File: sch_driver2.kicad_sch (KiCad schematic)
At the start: 16 parts, among them Q2 PSMN4R0-30YLDX, U1 ADA4099-2xR, U12 TS5A3159ADCK, U22 OPA333

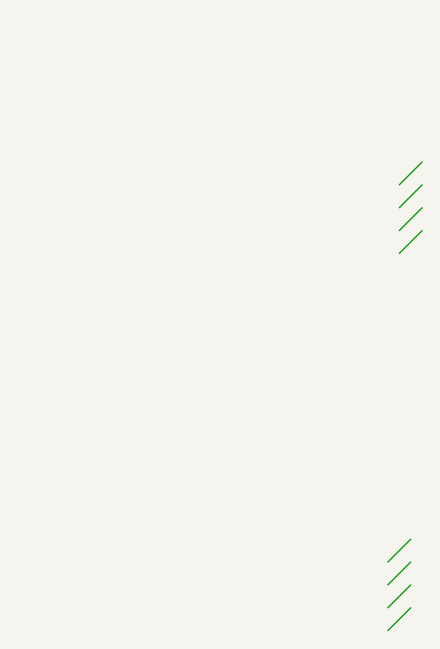
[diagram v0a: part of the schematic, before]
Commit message: Finished schematic refactor to six A-sheets. Updated PCB.
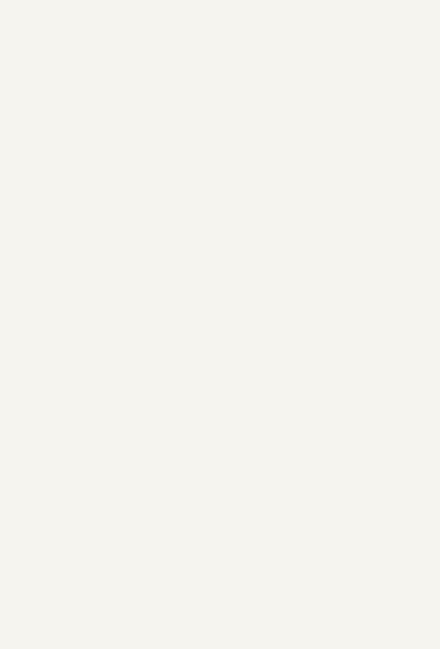
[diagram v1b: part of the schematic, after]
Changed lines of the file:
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@@
 	(title_block
 		(title "PBM Driver 4 V2")
-		(date "23-DEC-2025")
+		(date "24-DEC-2025")
 		(rev "A")
 		(comment 1 "Part Number: PCB104 Rev A")
@@
 		(color 0 0 0 0)
 	)
-	(bus_entry
-		(at 389.89 226.06)
-		(size -2.54 2.54)
-		(stroke
-			(width 0)
-			(type default)
-		)
-	)
-	(bus_entry
-		(at 389.89 223.52)
-		(size -2.54 2.54)
-		(stroke
-			(width 0)
-			(type default)
-		)
-	)
-	(bus_entry
-		(at 391.16 181.61)
-		(size -2.54 2.54)
-		(stroke
-			(width 0)
-			(type default)
-		)
-	)
-	(bus_entry
-		(at 391.16 179.07)
-		(size -2.54 2.54)
-		(stroke
-			(width 0)
-			(type default)
-		)
-	)
-	(bus_entry
-		(at 389.89 220.98)
-		(size -2.54 2.54)
-		(stroke
-			(width 0)
-			(type default)
-		)
-	)
-	(bus_entry
-		(at 391.16 184.15)
-		(size -2.54 2.54)
-		(stroke
-			(width 0)
-			(type default)
-		)
-	)
-	(bus_entry
-		(at 391.16 176.53)
-		(size -2.54 2.54)
-		(stroke
-			(width 0)
-			(type default)
-		)
-	)
-	(bus_entry
-		(at 389.89 218.44)
-		(size -2.54 2.54)
-		(stroke
-			(width 0)
-			(type default)
-		)
-	)
 	(wire

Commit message: Routing WIP. Prep to look at SOT-23 op amps for U1 and U2. Added convenience link to Git Bash.
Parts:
- added U4: ADA4099-2xR, Package_TO_SOT_SMD:TSOT-23-6, symbol Amplifier_Operational:ADA4099-1xUJ
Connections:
- net FB: now also U4.4 (-)
- net GND: now also U4.2 (V-)
- net REF: now also U4.3 (+)
- net OUT: now reaches C32.2, R12.1, U1.7
- net OUT: now also U4.1
- new net +12V: U4.6 (V+)

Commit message: Routing WIP with SOT-23 op amps
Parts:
- added C52: 100pF, $Local:C_0603_1608Metric, symbol $Local:C
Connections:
- net DAC: now also C52.1
- net GND: now also U4.5 (~{SHDN}), C52.2
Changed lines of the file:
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@@
+	)
+	(junction
+		(at 33.02 48.26)
+		(diameter 0)
+		(color 0 0 0 0)
+	)
+	(junction
+		(at 99.06 111.76)
+		(diameter 0)
+		(color 0 0 0 0)
 	)
 	(junction
@@
 	(wire
 		(pts
-			(xy 35.56 40.64) (xy 41.91 40.64)
+			(xy 27.94 40.64) (xy 41.91 40.64)
 		)
 		(stroke
@@
 	(wire
 		(pts
-			(xy 35.56 48.26) (xy 57.15 48.26)
+			(xy 27.94 48.26) (xy 33.02 48.26)
 		)
 		(stroke
@@
 	(wire
 		(pts
+			(xy 33.02 48.26) (xy 57.15 48.26)
+		)
+		(stroke
+			(width 0)
+			(type default)
+		)
+	)
+	(wire
+		(pts
+			(xy 33.02 68.58) (xy 33.02 71.12)
+		)
+		(stroke
+			(width 0)
+			(type default)
+		)
+	)
+	(wire
+		(pts
 			(xy 223.52 71.12) (xy 226.06 71.12)
 		)
@@
 	(wire
 		(pts
+			(xy 99.06 111.76) (xy 101.6 111.76)
+		)
+		(stroke
+			(width 0)
+			(type default)
+		)
+	)
+	(wire
+		(pts
 			(xy 54.61 55.88) (xy 54.61 53.34)
+		)
+		(stroke
+			(width 0)
+			(type default)
+		)
+	)
+	(wire
+		(pts
+			(xy 33.02 48.26) (xy 33.02 60.96)
 		)
 		(stroke
@@
 	(hierarchical_label "DAC"
 		(shape input)
-		(at 35.56 48.26 180)
+		(at 27.94 48.26 180)
 		(effects
 			(font
@@
 	(hierarchical_label "SEL"
 		(shape input)
-		(at 35.56 40.64 180)
+		(at 27.94 40.64 180)
 		(effects
 			(font
@@
 	)
 	(symbol
+		(lib_id "$Local:GND")
+		(at 33.02 71.12 0)
+		(unit 1)
+		(exclude_from_sim no)
+		(in_bom yes)
+		(on_board yes)
+		(dnp no)
+		(fields_autoplaced yes)
+		(property "Reference" "#PWR022"
+			(at 33.02 77.47 0)
+			(effects
+				(font
+					(size 1.27 1.27)
+				)
+				(hide yes)
+			)
+		)
+		(property "Value" "GND"
+			(at 33.02 76.2 0)
+			(effects
+				(font
+					(size 1.27 1.27)
+				)
+			)
+		)
+		(property "Footprint" ""
+			(at 33.02 71.12 0)
+			(effects
+				(font
+					(size 1.27 1.27)
+				)
+				(hide yes)
+			)
+		)
+		(property "Datasheet" ""
+			(at 33.02 71.12 0)
+			(effects
+				(font
+					(size 1.27 1.27)
+				)
+				(hide yes)
+			)
+		)
+		(property "Description" "Power symbol creates a global label with name \"GND\" , ground"
+			(at 33.02 71.12 0)
+			(effects
+				(font
+					(size 1.27 1.27)
+				)
+				(hide yes)
+			)
+		)
+		(pin "1"
+		)
+		(instances
+			(project "pbm_driver4_v2"
+				(path "/04797749-7aaf-42f7-a5f4-0b9aeb0ad7be/4a4bbbb0-66db-4dbb-adf8-ecfc17002d21"
+					(reference "#PWR022")
+					(unit 1)
+				)
+			)
+		)
+	)
+	(symbol
 		(lib_id "$Local:R_0603_10K")
 		(at 199.39 88.9 270)
@@
 					(unit 1)
 				)
+			)
+		)
+	)
+	(symbol
+		(lib_id "$Local:C")
+		(at 33.02 64.77 0)
+		(unit 1)
+		(exclude_from_sim no)
+		(in_bom yes)
+		(on_board yes)
+		(dnp no)
+		(property "Reference" "C52"
+			(at 29.21 63.4999 0)
+			(effects
+				(font
+					(size 1.27 1.27)
+				)
+				(justify right)
+			)
+		)
+		(property "Value" "100pF"
+			(at 29.21 66.0399 0)
+			(effects
+				(font
+					(size 1.27 1.27)
+				)
+				(justify right)
+			)
+		)
+		(property "Footprint" "$Local:C_0603_1608Metric"
+			(at 33.9852 68.58 0)
+			(effects
+				(font
+					(size 1.27 1.27)
+				)
+				(hide yes)
+			)
+		)
+		(property "Datasheet" "~"
+			(at 33.02 64.77 0)
+			(effects
+				(font
+					(size 1.27 1.27)
+				)
+				(hide yes)
+			)
+		)
+		(property "Description" "Unpolarized capacitor"
+			(at 33.02 64.77 0)
+			(effects
+				(font
+					(size 1.27 1.27)
+				)
+				(hide yes)
+			)
+		)
+		(pin "2"
+		)
+		(pin "1"
+		)
+		(instances
+			(project "pbm_driver4_v2"
+				(path "/04797749-7aaf-42f7-a5f4-0b9aeb0ad7be/4a4bbbb0-66db-4dbb-adf8-ecfc17002d21"
+					(reference "C52")
+					(unit 1)
+				)

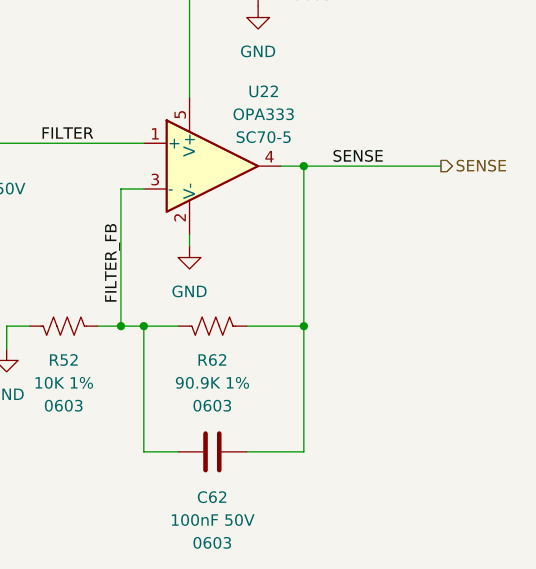
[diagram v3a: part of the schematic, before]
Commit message: Added pull-downs to output of Sense filter op amps
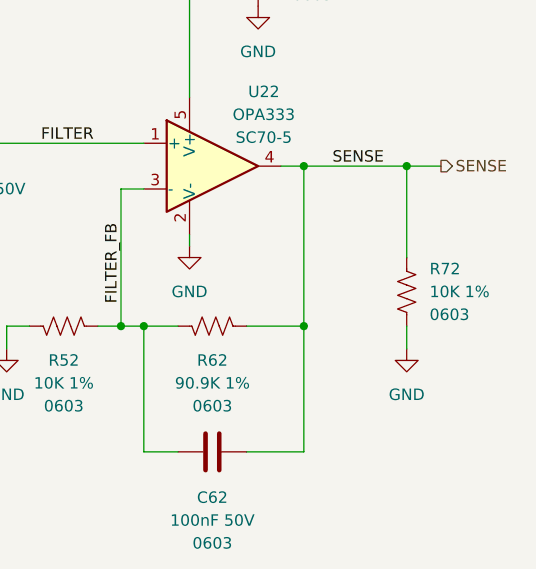
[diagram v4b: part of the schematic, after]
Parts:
- added R72: 10K 1%, $Local:R_0603_1608Metric, symbol $Local:R_0603_10K
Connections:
- net GND: now also R72.2
- net SENSE: now also R72.1
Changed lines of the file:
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@@
+	)
+	(junction
+		(at 237.49 71.12)
+		(diameter 0)
+		(color 0 0 0 0)
 	)
 	(junction
@@
 	(wire
 		(pts
+			(xy 237.49 88.9) (xy 237.49 91.44)
+		)
+		(stroke
+			(width 0)
+			(type default)
+		)
+	)
+	(wire
+		(pts
 			(xy 118.11 177.8) (xy 95.25 177.8)
 		)
@@
 	(wire
 		(pts
+			(xy 237.49 71.12) (xy 237.49 81.28)
+		)
+		(stroke
+			(width 0)
+			(type default)
+		)
+	)
+	(wire
+		(pts
 			(xy 41.91 60.96) (xy 41.91 40.64)
 		)
@@
 	(wire
 		(pts
+			(xy 237.49 71.12) (xy 241.3 71.12)
+		)
+		(stroke
+			(width 0)
+			(type default)
+		)
+	)
+	(wire
+		(pts
 			(xy 64.77 40.64) (xy 64.77 43.18)
 		)
@@
 	(wire
 		(pts
-			(xy 226.06 71.12) (xy 241.3 71.12)
+			(xy 226.06 71.12) (xy 237.49 71.12)
 		)
 		(stroke
@@
 				(path "/04797749-7aaf-42f7-a5f4-0b9aeb0ad7be/4a4bbbb0-66db-4dbb-adf8-ecfc17002d21"
 					(reference "#PWR28")
+					(unit 1)
+				)
+			)
+		)
+	)
+	(symbol
+		(lib_id "$Local:R_0603_10K")
+		(at 237.49 85.09 0)
+		(unit 1)
+		(exclude_from_sim no)
+		(in_bom yes)
+		(on_board yes)
+		(dnp no)
+		(fields_autoplaced yes)
+		(property "Reference" "R72"
+			(at 240.03 82.5499 0)
+			(effects
+				(font
+					(size 1.27 1.27)
+				)
+				(justify left)
+			)
+		)
+		(property "Value" "10K 1%"
+			(at 240.03 85.0899 0)
+			(effects
+				(font
+					(size 1.27 1.27)
+				)
+				(justify left)
+			)
+		)
+		(property "Footprint" "$Local:R_0603_1608Metric"
+			(at 238.506 85.344 90)
+			(effects
+				(font
+					(size 1.27 1.27)
+				)
+				(hide yes)
+			)
+		)
+		(property "Datasheet" "~"
+			(at 237.49 85.09 0)
+			(effects
+				(font
+					(size 1.27 1.27)
+				)
+				(hide yes)
+			)
+		)
+		(property "Description" "RES SMD 10K OHM 1% 1/10W 0603"
+			(at 237.49 85.09 0)
+			(effects
+				(font
+					(size 1.27 1.27)
+				)
+				(hide yes)
+			)
+		)
+		(property "Size" "0603"
+			(at 240.03 87.6299 0)
+			(effects
+				(font
+					(size 1.27 1.27)
+				)
+				(justify left)
+			)
+		)
+		(property "PN" ""
+			(at 237.49 85.09 0)
+			(effects
+				(font
+					(size 1.27 1.27)
+				)
+				(hide yes)
+			)
+		)
+		(pin "1"
+		)
+		(pin "2"
+		)
+		(instances
+			(project "pbm_driver4_v2"
+				(path "/04797749-7aaf-42f7-a5f4-0b9aeb0ad7be/4a4bbbb0-66db-4dbb-adf8-ecfc17002d21"
+					(reference "R72")
 					(unit 1)
 				)
@@
 					(unit 1)
 				)
+			)
+		)
+	)
+	(symbol
+		(lib_id "$Local:GND")
+		(at 237.49 91.44 0)
+		(unit 1)
+		(exclude_from_sim no)
+		(in_bom yes)
+		(on_board yes)
+		(dnp no)
+		(fields_autoplaced yes)
+		(property "Reference" "#PWR035"
+			(at 237.49 97.79 0)
+			(effects
+				(font
+					(size 1.27 1.27)
+				)
+				(hide yes)
+			)
+		)
+		(property "Value" "GND"
+			(at 237.49 96.52 0)
+			(effects
+				(font
+					(size 1.27 1.27)
+				)
+			)
+		)
+		(property "Footprint" ""
+			(at 237.49 91.44 0)
+			(effects
+				(font
+					(size 1.27 1.27)
+				)
+				(hide yes)
+			)
+		)
+		(property "Datasheet" ""
+			(at 237.49 91.44 0)
+			(effects
+				(font
+					(size 1.27 1.27)
+				)
+				(hide yes)
+			)
+		)
+		(property "Description" "Power symbol creates a global label with name \"GND\" , ground"
+			(at 237.49 91.44 0)
+			(effects
+				(font
+					(size 1.27 1.27)
+				)
+				(hide yes)
+			)
+		)
+		(pin "1"
+		)
+		(instances
+			(project "pbm_driver4_v2"
+				(path "/04797749-7aaf-42f7-a5f4-0b9aeb0ad7be/4a4bbbb0-66db-4dbb-adf8-ecfc17002d21"
+					(reference "#PWR035")
+					(unit 1)
+				)

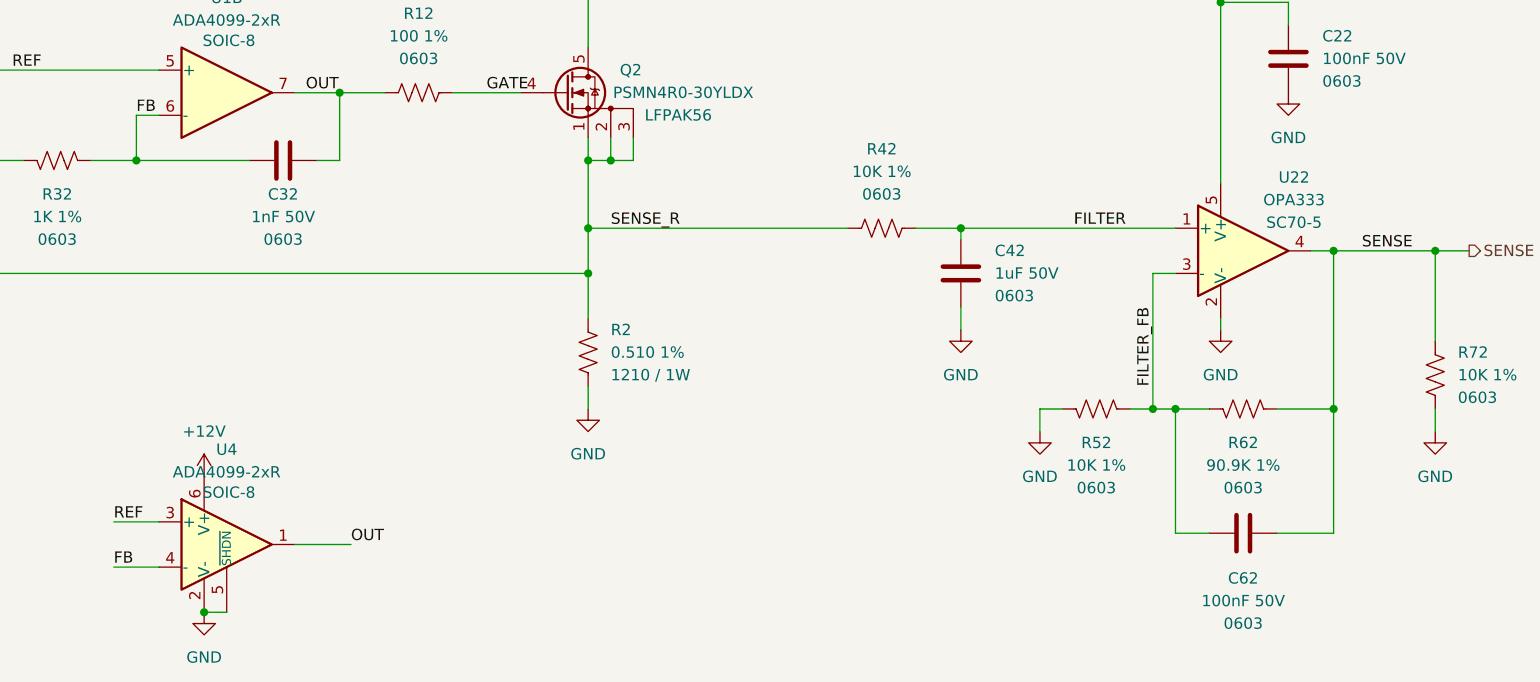
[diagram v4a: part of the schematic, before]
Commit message: Change schematic sense buffer vrom OPA333 in SC70 to OPA365 in SOT-23
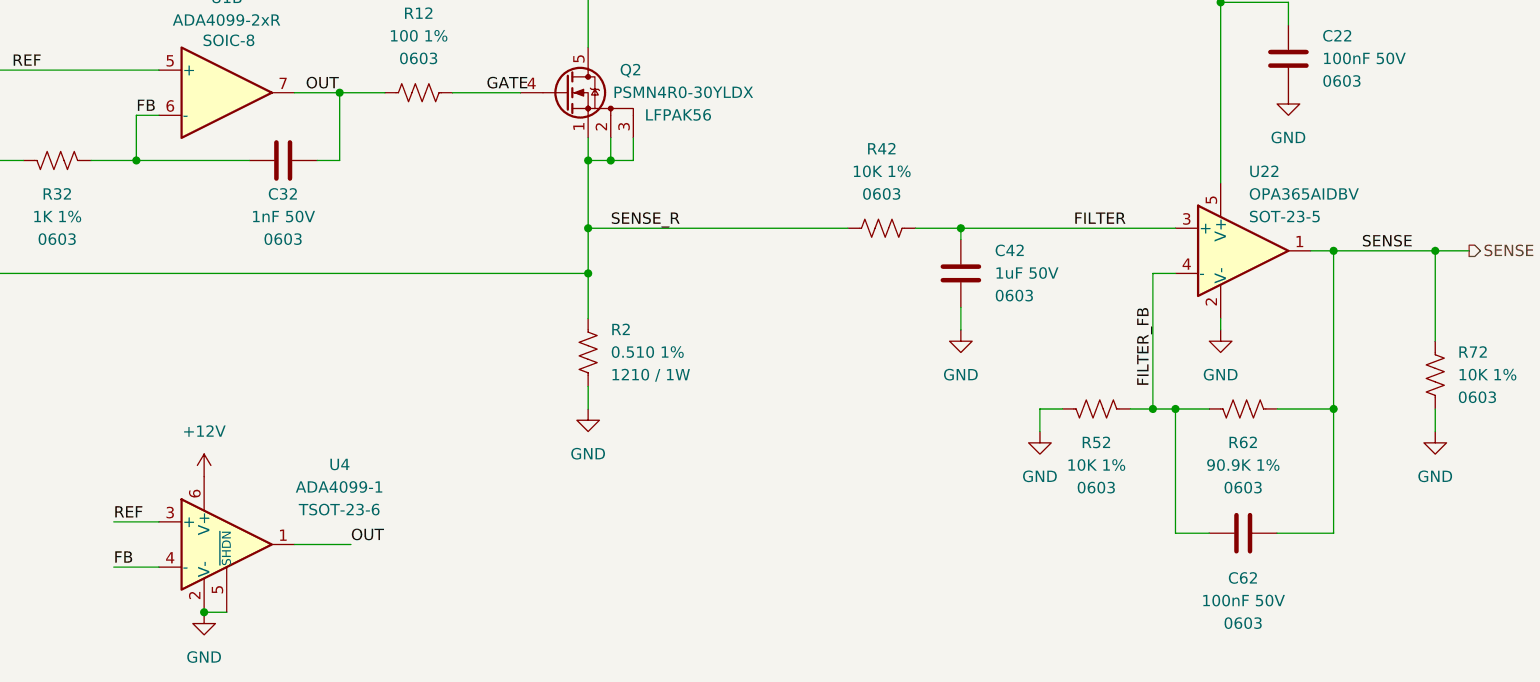
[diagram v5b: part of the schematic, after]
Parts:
- removed U22: OPA333, Package_TO_SOT_SMD:SOT-353_SC-70-5, symbol $Local:OPA333
- removed U4: ADA4099-2xR, Package_TO_SOT_SMD:TSOT-23-6, symbol Amplifier_Operational:ADA4099-1xUJ
- added U22: OPA365AIDBV, $Local:SOT-23-5, symbol $Local:OPA365AIDBV
- added U4: ADA4099-1, $Local:TSOT-23-6, symbol $Local:ADA4099-1
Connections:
- net +12V: now also U4.6 (V+)
- net +3.3V: now also U22.5 (V+)
- net FB: now also U4.4 (-)
- net FILTER: now also U22.3 (+)
- net FILTER_FB: now also U22.4 (-)
- net GND: now also U22.2 (V-), U4.2 (V-), U4.5 (~{SHDN})
- net OUT: now also U4.1
- net REF: now also U4.3 (+)
- net SENSE: now also U22.1
